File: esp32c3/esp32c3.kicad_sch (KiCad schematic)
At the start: 29 parts, among them J1 A1501WR-S-2P, J2 Conn_01x06, J3 Conn_01x05, SW1 wake up, U1 ESP32-C3-WROOM-02, U2 AHT10, U3 LIS2DH, U4 HX6306

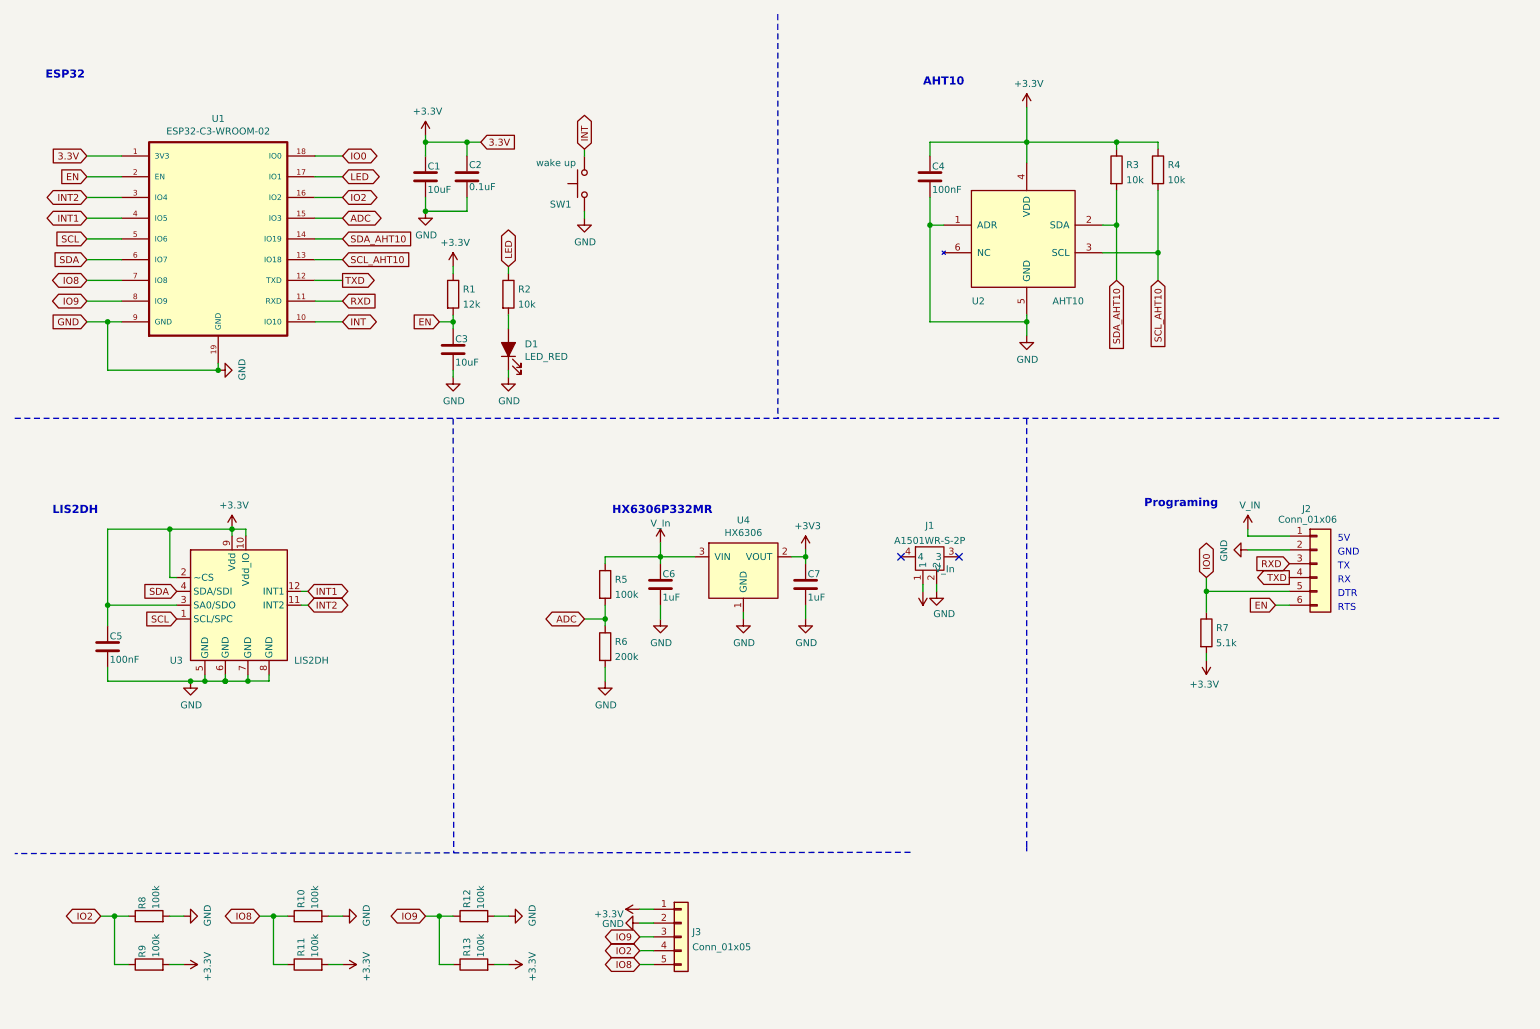
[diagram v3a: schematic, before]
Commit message: Place components on one side
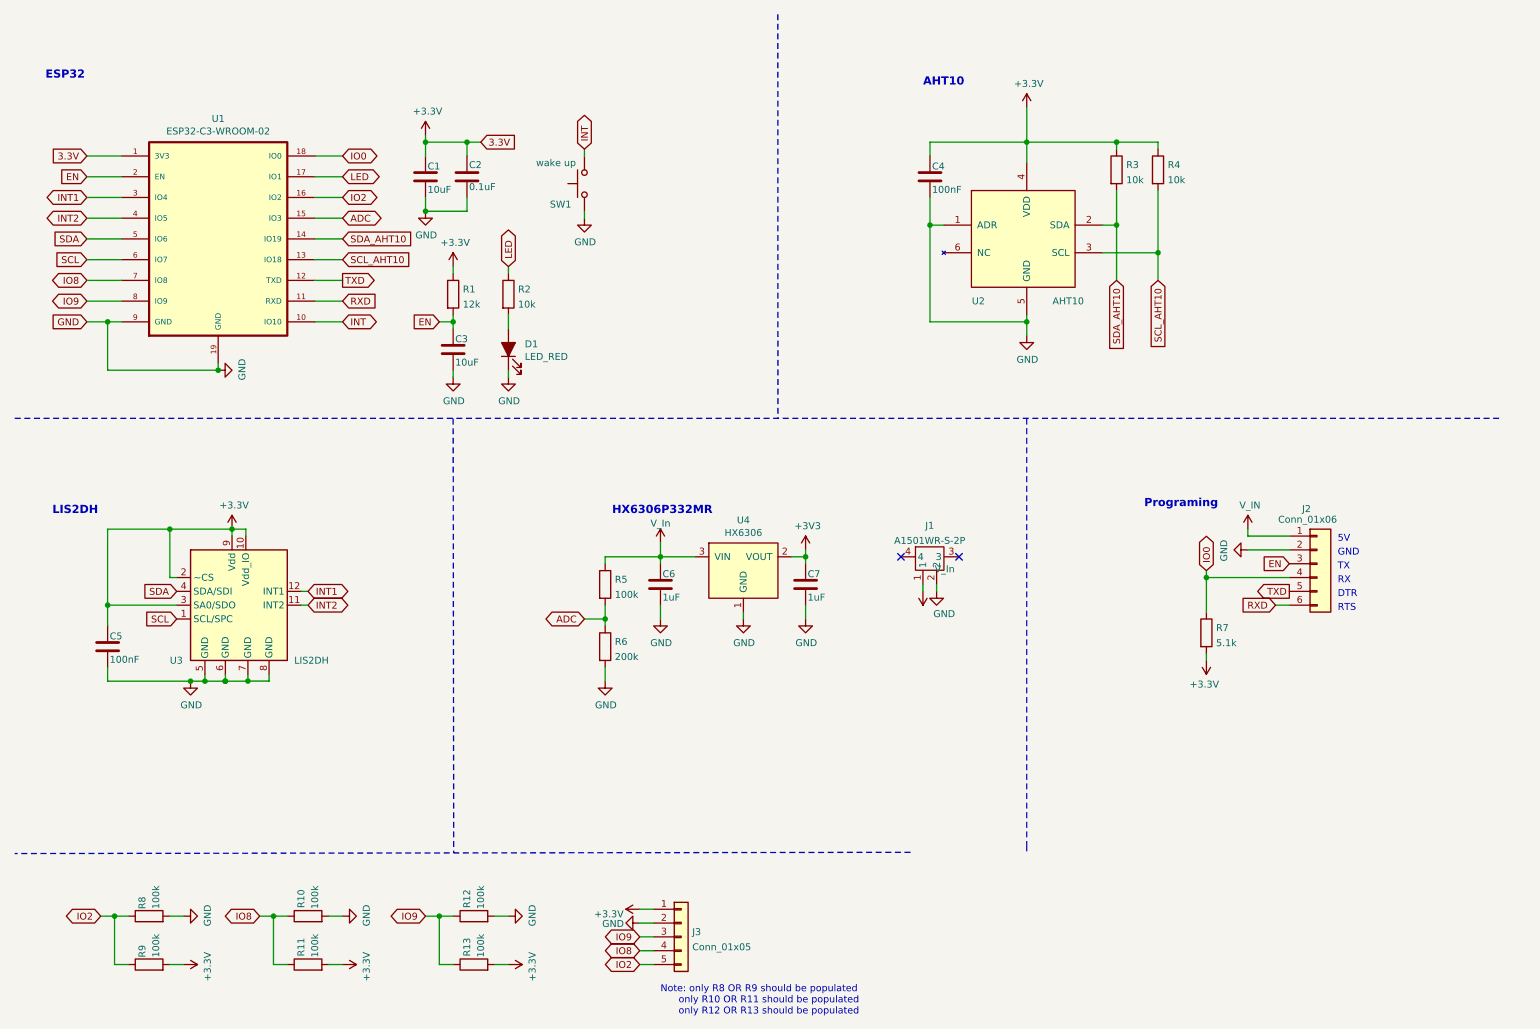
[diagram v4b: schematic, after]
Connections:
- net EN: now also J2.3 (Pin_3); no longer J2.6 (Pin_6)
- net INT1: now also U1.3 (IO4); no longer U1.4 (IO5)
- net INT2: now also U1.4 (IO5); no longer U1.3 (IO4)
- net IO0: now also J2.4 (Pin_4); no longer J2.5 (Pin_5)
- net IO2: now also J3.5 (Pin_5); no longer J3.4 (Pin_4)
- net IO8: now also J3.4 (Pin_4); no longer J3.5 (Pin_5)
- net RXD: now also J2.6 (Pin_6); no longer J2.3 (Pin_3)
- net SCL: now also U1.6 (IO7); no longer U1.5 (IO6)
- net SDA: now also U1.5 (IO6); no longer U1.6 (IO7)
- net TXD: now also J2.5 (Pin_5); no longer J2.4 (Pin_4)
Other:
- note added: "Note: only R8 OR R9 should be populated only R10 OR R11 should be populated only R12 OR R13 should be populated"
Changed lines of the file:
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@@
   (junction (at 214.63 50.8) (diameter 1.016) (color 0 0 0 0))
   (junction (at 222.25 55.88) (diameter 1.016) (color 0 0 0 0))
-  (junction (at 231.14 118.11) (diameter 1.016) (color 0 0 0 0))
+  (junction (at 231.14 115.57) (diameter 1.016) (color 0 0 0 0))
   (no_connect (at 175.006 111.76))
   (no_connect (at 185.674 111.76))
@@
     (stroke (width 0) (type solid) (color 0 0 0 0))
   )
-  (wire (pts (xy 231.14 115.57) (xy 231.14 118.11))
-    (stroke (width 0) (type solid) (color 0 0 0 0))
-  )
-  (wire (pts (xy 231.14 118.11) (xy 231.14 121.92))
-    (stroke (width 0) (type solid) (color 0 0 0 0))
-  )
-  (wire (pts (xy 231.14 118.11) (xy 246.38 118.11))
+  (wire (pts (xy 231.14 114.3) (xy 231.14 115.57))
+    (stroke (width 0) (type solid) (color 0 0 0 0))
+  )
+  (wire (pts (xy 231.14 115.57) (xy 231.14 121.92))
+    (stroke (width 0) (type solid) (color 0 0 0 0))
+  )
+  (wire (pts (xy 231.14 115.57) (xy 246.38 115.57))
     (stroke (width 0) (type solid) (color 0 0 0 0))
   )
@@
     (effects (font (size 1.4986 1.4986) (thickness 0.2997) bold) (justify left bottom))
   )
+  (text "Note: only R8 OR R9 should be populated\n	  only R10 OR R11 should be populated\n	  only R12 OR R13 should be populated\n"
+    (at 130.81 196.088 0)
+    (effects (font (size 1.27 1.27)) (justify left bottom))
+  )
   (text "AHT10" (at 179.07 25.4 0)
     (effects (font (size 1.4986 1.4986) (thickness 0.2997) bold) (justify left bottom))
@@
     )
   )
-  (global_label "INT2" (shape bidirectional) (at 25.4 45.72 180) (fields_autoplaced)
+  (global_label "INT1" (shape bidirectional) (at 25.4 45.72 180) (fields_autoplaced)
     (effects (font (size 1.27 1.27)) (justify right))
     (property "Intersheet References" "${INTERSHEET_REFS}" (id 0) (at 18.8745 45.6406 0)
@@
     )
   )
-  (global_label "INT1" (shape bidirectional) (at 25.4 49.53 180) (fields_autoplaced)
+  (global_label "INT2" (shape bidirectional) (at 25.4 49.53 180) (fields_autoplaced)
     (effects (font (size 1.27 1.27)) (justify right))
     (property "Intersheet References" "${INTERSHEET_REFS}" (id 0) (at 18.8745 49.4506 0)
@@
     )
   )
-  (global_label "SCL" (shape input) (at 25.4 53.34 180) (fields_autoplaced)
-    (effects (font (size 1.27 1.27)) (justify right))
-    (property "Intersheet References" "${INTERSHEET_REFS}" (id 0) (at 121.92 -13.97 0)
-      (effects (font (size 1.27 1.27)) hide)
-    )
-  )
-  (global_label "SDA" (shape input) (at 25.4 57.15 180) (fields_autoplaced)
-    (effects (font (size 1.27 1.27)) (justify right))
-    (property "Intersheet References" "${INTERSHEET_REFS}" (id 0) (at 121.92 -2.54 0)
+  (global_label "SDA" (shape input) (at 25.4 53.34 180) (fields_autoplaced)
+    (effects (font (size 1.27 1.27)) (justify right))
+    (property "Intersheet References" "${INTERSHEET_REFS}" (id 0) (at 121.92 -6.35 0)
+      (effects (font (size 1.27 1.27)) hide)
+    )
+  )
+  (global_label "SCL" (shape input) (at 25.4 57.15 180) (fields_autoplaced)
+    (effects (font (size 1.27 1.27)) (justify right))
+    (property "Intersheet References" "${INTERSHEET_REFS}" (id 0) (at 121.92 -10.16 0)
       (effects (font (size 1.27 1.27)) hide)
     )
@@
     )
   )
-  (global_label "IO2" (shape bidirectional) (at 127 184.15 180) (fields_autoplaced)
-    (effects (font (size 1.27 1.27)) (justify right))
-    (property "Intersheet References" "${INTERSHEET_REFS}" (id 0) (at 121.4421 184.2294 0)
-      (effects (font (size 1.27 1.27)) (justify right) hide)
-    )
-  )
-  (global_label "IO8" (shape bidirectional) (at 127 186.69 180) (fields_autoplaced)
-    (effects (font (size 1.27 1.27)) (justify right))
-    (property "Intersheet References" "${INTERSHEET_REFS}" (id 0) (at 121.4421 186.6106 0)
+  (global_label "IO8" (shape bidirectional) (at 127 184.15 180) (fields_autoplaced)
+    (effects (font (size 1.27 1.27)) (justify right))
+    (property "Intersheet References" "${INTERSHEET_REFS}" (id 0) (at 121.4421 184.0706 0)
+      (effects (font (size 1.27 1.27)) (justify right) hide)
+    )
+  )
+  (global_label "IO2" (shape bidirectional) (at 127 186.69 180) (fields_autoplaced)
+    (effects (font (size 1.27 1.27)) (justify right))
+    (property "Intersheet References" "${INTERSHEET_REFS}" (id 0) (at 121.4421 186.7694 0)
       (effects (font (size 1.27 1.27)) (justify right) hide)
     )
@@
     )
   )
-  (global_label "IO0" (shape bidirectional) (at 231.14 115.57 90) (fields_autoplaced)
-    (effects (font (size 1.27 1.27)) (justify left))
-    (property "Intersheet References" "${INTERSHEET_REFS}" (id 0) (at 160.02 274.32 0)
-      (effects (font (size 1.27 1.27)) hide)
-    )
-  )
-  (global_label "EN" (shape input) (at 243.84 120.65 180) (fields_autoplaced)
-    (effects (font (size 1.27 1.27)) (justify right))
-    (property "Intersheet References" "${INTERSHEET_REFS}" (id 0) (at 299.72 229.87 0)
-      (effects (font (size 1.27 1.27)) hide)
-    )
-  )
-  (global_label "RXD" (shape input) (at 246.38 113.03 180) (fields_autoplaced)
-    (effects (font (size 1.27 1.27)) (justify right))
-    (property "Intersheet References" "${INTERSHEET_REFS}" (id 0) (at 405.13 210.82 0)
-      (effects (font (size 1.27 1.27)) hide)
-    )
-  )
-  (global_label "TXD" (shape output) (at 246.38 115.57 180) (fields_autoplaced)
-    (effects (font (size 1.27 1.27)) (justify right))
-    (property "Intersheet References" "${INTERSHEET_REFS}" (id 0) (at 405.13 209.55 0)
-      (effects (font (size 1.27 1.27)) hide)
-    )
+  (global_label "IO0" (shape bidirectional) (at 231.14 114.3 90) (fields_autoplaced)
+    (effects (font (size 1.27 1.27)) (justify left))
+    (property "Intersheet References" "${INTERSHEET_REFS}" (id 0) (at 160.02 273.05 0)
+      (effects (font (size 1.27 1.27)) hide)
+    )
+  )
+  (global_label "RXD" (shape input) (at 243.84 120.65 180) (fields_autoplaced)
+    (effects (font (size 1.27 1.27)) (justify right))
+    (property "Intersheet References" "${INTERSHEET_REFS}" (id 0) (at 402.59 218.44 0)
+      (effects (font (size 1.27 1.27)) hide)
+    )
+  )
+  (global_label "EN" (shape input) (at 246.38 113.03 180) (fields_autoplaced)
+    (effects (font (size 1.27 1.27)) (justify right))
+    (property "Intersheet References" "${INTERSHEET_REFS}" (id 0) (at 302.26 222.25 0)
+      (effects (font (size 1.27 1.27)) hide)
+    )
+  )
+  (global_label "TXD" (shape output) (at 246.38 118.11 180) (fields_autoplaced)
+    (effects (font (size 1.27 1.27)) (justify right))
+    (property "Intersheet References" "${INTERSHEET_REFS}" (id 0) (at 405.13 212.09 0)
+      (effects (font (size 1.27 1.27)) hide)
+    )
